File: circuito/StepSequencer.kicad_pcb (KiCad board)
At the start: 2 copper layers, 83 parts, among them P1 BEAGLEBONE_BLACK, SW1 SW_PUSH, SW10 SW_PUSH, SW11 SW_PUSH, SW12 SW_PUSH, SW13 SW_PUSH, SW14 SW_PUSH, SW15 SW_PUSH, SW16 SW_PUSH, SW2 SW_PUSH, SW3 SW_PUSH, SW4 SW_PUSH, SW5 SW_PUSH, SW6 SW_PUSH, SW7 SW_PUSH, SW8 SW_PUSH, SW9 SW_PUSH

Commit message: Empezando layout del pcb
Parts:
- removed D1, D10, D11, D12, D13, D14, D15, D16, D17, D18, D19, D2, D20, D21, D22, D23, D24, D25, D26, D27, D28, D29, D3, D30, D31, D32, D4, D5, D6, D7, D8, D9: LED, LEDs:LED-5MM
- removed R1, R10, R11, R12, R13, R14, R15, R16, R17, R18, R19, R2, R20, R21, R22, R23, R24, R25, R26, R27, R28, R29, R3, R30, R31, R32, R4, R5, R6, R7, R8, R9: R, Resistors_ThroughHole:Resistor_Horizontal_RM10mm
- removed SW16: SW_PUSH, Buttons_Switches_ThroughHole:SW_PUSH-12mm
- added D1_0 (x2): LED, LEDs:LED-5MM, F.Cu at (157.2, 152.4)
- added D1_1: LED, LEDs:LED-5MM, F.Cu at (170.0, 153.0)
- added D1_10, D1_11, D1_12, D1_8, D1_9: LED, LEDs:LED-5MM, F.Cu at (128.7, 83.1)
- added D1_13: LED, LEDs:LED-5MM, F.Cu at (128.0, 84.0)
- added D1_14, D1_15: LED, LEDs:LED-5MM, F.Cu at (130.0, 84.0)
- added D1_2: LED, LEDs:LED-5MM, F.Cu at (183.0, 152.0)
- added D1_3: LED, LEDs:LED-5MM, F.Cu at (197.0, 153.0)
- added D1_4: LED, LEDs:LED-5MM, F.Cu at (211.0, 152.0)
- added D1_5: LED, LEDs:LED-5MM, F.Cu at (225.0, 152.0)
- added D1_6: LED, LEDs:LED-5MM, F.Cu at (239.0, 152.0)
- added D1_7: LED, LEDs:LED-5MM, F.Cu at (253.0, 152.0)
- added D2_0: LED, LEDs:LED-5MM, F.Cu at (123.0, 154.0)
- added D2_1, D2_10, D2_11, D2_12, D2_13, D2_14, D2_15, D2_2, D2_3, D2_4, D2_5, D2_6, D2_7, D2_8, D2_9: LED, LEDs:LED-5MM, F.Cu at (128.8, 83.5)
- added R1_0: R, Resistors_ThroughHole:Resistor_Horizontal_RM10mm, F.Cu at (156.0, 157.2)
- added R1_1: R, Resistors_ThroughHole:Resistor_Horizontal_RM10mm, F.Cu at (171.0, 157.0)
- added R1_10, R1_11, R1_12, R1_13, R1_14, R1_15, R1_8, R1_9, R2_1, R2_10, R2_11, R2_12, R2_13, R2_14, R2_15, R2_2, R2_3, R2_4, R2_5, R2_6, R2_7, R2_8, R2_9: R, Resistors_ThroughHole:Resistor_Horizontal_RM10mm, F.Cu at (127.0, 75.0)
- added R1_2: R, Resistors_ThroughHole:Resistor_Horizontal_RM10mm, F.Cu at (185.0, 157.0)
- added R1_3: R, Resistors_ThroughHole:Resistor_Horizontal_RM10mm, F.Cu at (199.0, 157.0)
- added R1_4: R, Resistors_ThroughHole:Resistor_Horizontal_RM10mm, F.Cu at (212.0, 157.0)
- added R1_5: R, Resistors_ThroughHole:Resistor_Horizontal_RM10mm, F.Cu at (227.0, 157.0)
- added R1_6: R, Resistors_ThroughHole:Resistor_Horizontal_RM10mm, F.Cu at (240.0, 157.0)
- added R1_7: R, Resistors_ThroughHole:Resistor_Horizontal_RM10mm, F.Cu at (254.0, 157.0)
- added R2_0: R, Resistors_ThroughHole:Resistor_Horizontal_RM10mm, F.Cu at (122.0, 148.2)
- added SW0: SW_PUSH, Buttons_Switches_ThroughHole:SW_PUSH-12mm, F.Cu at (156.0, 140.8)
- RV1, RV2: footprint Potentiometers:Potentiometer_Alps-RK163-single_20mm -> StepSequencer:POT_AZUL
- moved RV1 124.6 mm to (99.5, 32.5)
- moved RV2 117.8 mm to (79.2, 32.5)
- moved SW2 103.4 mm to (169.9, 140.8), turned to 90 degrees
- moved P1 92.9 mm to (158.0, 126.0), turned to 0 degrees
- moved SW4 84.9 mm to (183.9, 140.8), turned to 90 degrees
- moved SW15 72.5 mm to (252.0, 98.9), turned to 90 degrees
- moved SW6 67.1 mm to (197.8, 140.8), turned to 90 degrees
- moved SW1 66.3 mm to (154.2, 98.9), turned to 90 degrees
- moved SW13 52.8 mm to (238.0, 98.9), turned to 90 degrees
- moved SW8 50.8 mm to (211.8, 140.8), turned to 90 degrees
- moved SW3 46.6 mm to (168.1, 98.9), turned to 90 degrees
- moved SW14 38.8 mm to (253.7, 140.8), turned to 90 degrees
- moved SW10 38.0 mm to (225.8, 140.8), turned to 90 degrees
- moved SW11 33.3 mm to (224.0, 98.9), turned to 90 degrees
- moved SW12 32.9 mm to (239.8, 140.8), turned to 90 degrees
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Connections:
- P1 pad A10: /led1_2 -> /led1_1
- P1 pad A11: /btn3 -> /btn2
- P1 pad A12: /led1_3 -> /led1_2
- P1 pad A13: /btn4 -> /btn3
- P1 pad A14: /led1_4 -> /led1_3
- P1 pad A15: /btn5 -> /btn4
- P1 pad A16: /led1_5 -> /led1_4
- P1 pad A17: /btn6 -> /btn5
- P1 pad A18: /led1_6 -> /led1_5
- P1 pad A19: /btn7 -> /btn6
- P1 pad A26: /led1_7 -> /led1_6
- P1 pad A27: /btn8 -> /btn7
- P1 pad A28: /led1_8 -> /led1_7
- P1 pad A29: /btn9 -> /btn8
- P1 pad A30: /led1_9 -> /led1_8
- P1 pad A31: /btn10 -> /btn9
- P1 pad A32: /led1_10 -> /led1_9
- P1 pad A33: /btn11 -> /btn10
- P1 pad A34: /led1_11 -> /led1_10
- P1 pad A35: /btn12 -> /btn11
- P1 pad A36: /led1_12 -> /led1_11
- P1 pad A37: /btn13 -> /btn12
- P1 pad A38: /led1_13 -> /led1_12
- P1 pad A39: /btn14 -> /btn13
- P1 pad A40: /led1_14 -> /led1_13
- P1 pad A41: /btn15 -> /btn14
- P1 pad A42: /led1_15 -> /led1_14
- P1 pad A43: /btn16 -> /btn15
- P1 pad A44: /led1_16 -> /led1_15
- P1 pad A7: /btn1 -> /btn0
- P1 pad A8: /led1_1 -> /led1_0
- P1 pad A9: /btn2 -> /btn1
- P1 pad B11: /led2_1 -> /led2_0
- P1 pad B12: /led2_9 -> /led2_8
- P1 pad B13: /led2_2 -> /led2_1
- P1 pad B14: /led2_10 -> /led2_9
- P1 pad B15: /led2_3 -> /led2_2
- P1 pad B16: /led2_11 -> /led2_10
- P1 pad B17: /led2_4 -> /led2_3
- P1 pad B18: /led2_12 -> /led2_11
- P1 pad B21: /led2_5 -> /led2_4
- P1 pad B22: /led2_13 -> /led2_12
- P1 pad B23: /led2_6 -> /led2_5
- P1 pad B24: /led2_14 -> /led2_13
- P1 pad B26: /led2_15 -> /led2_14
- P1 pad B27: /led2_7 -> /led2_6
- P1 pad B30: /led2_16 -> /led2_15
- P1 pad B38: /pot2 -> /pot1
- P1 pad B40: /pot1 -> /pot0
- P1 pad B41: /led2_8 -> /led2_7
- RV1 pad 2: /pot1 -> /pot0
- RV2 pad 2: /pot2 -> /pot1

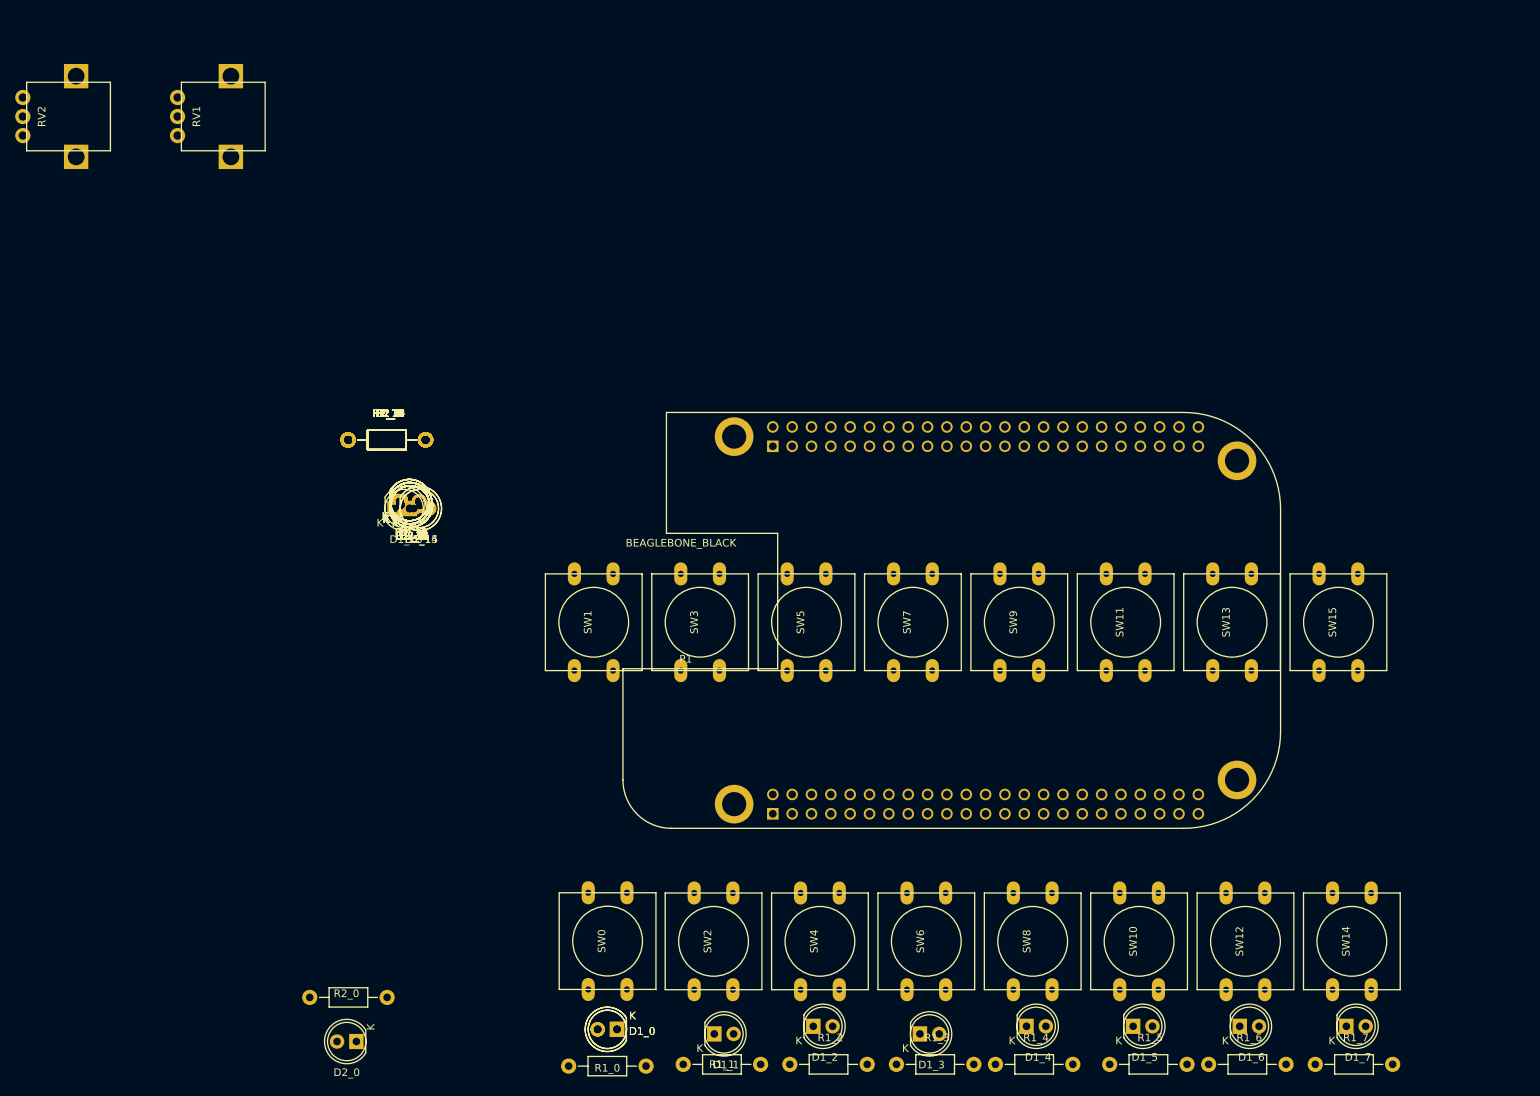
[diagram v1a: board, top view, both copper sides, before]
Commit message: PBC ruteado de leds, botones, beagle, faltan pots y tierras.
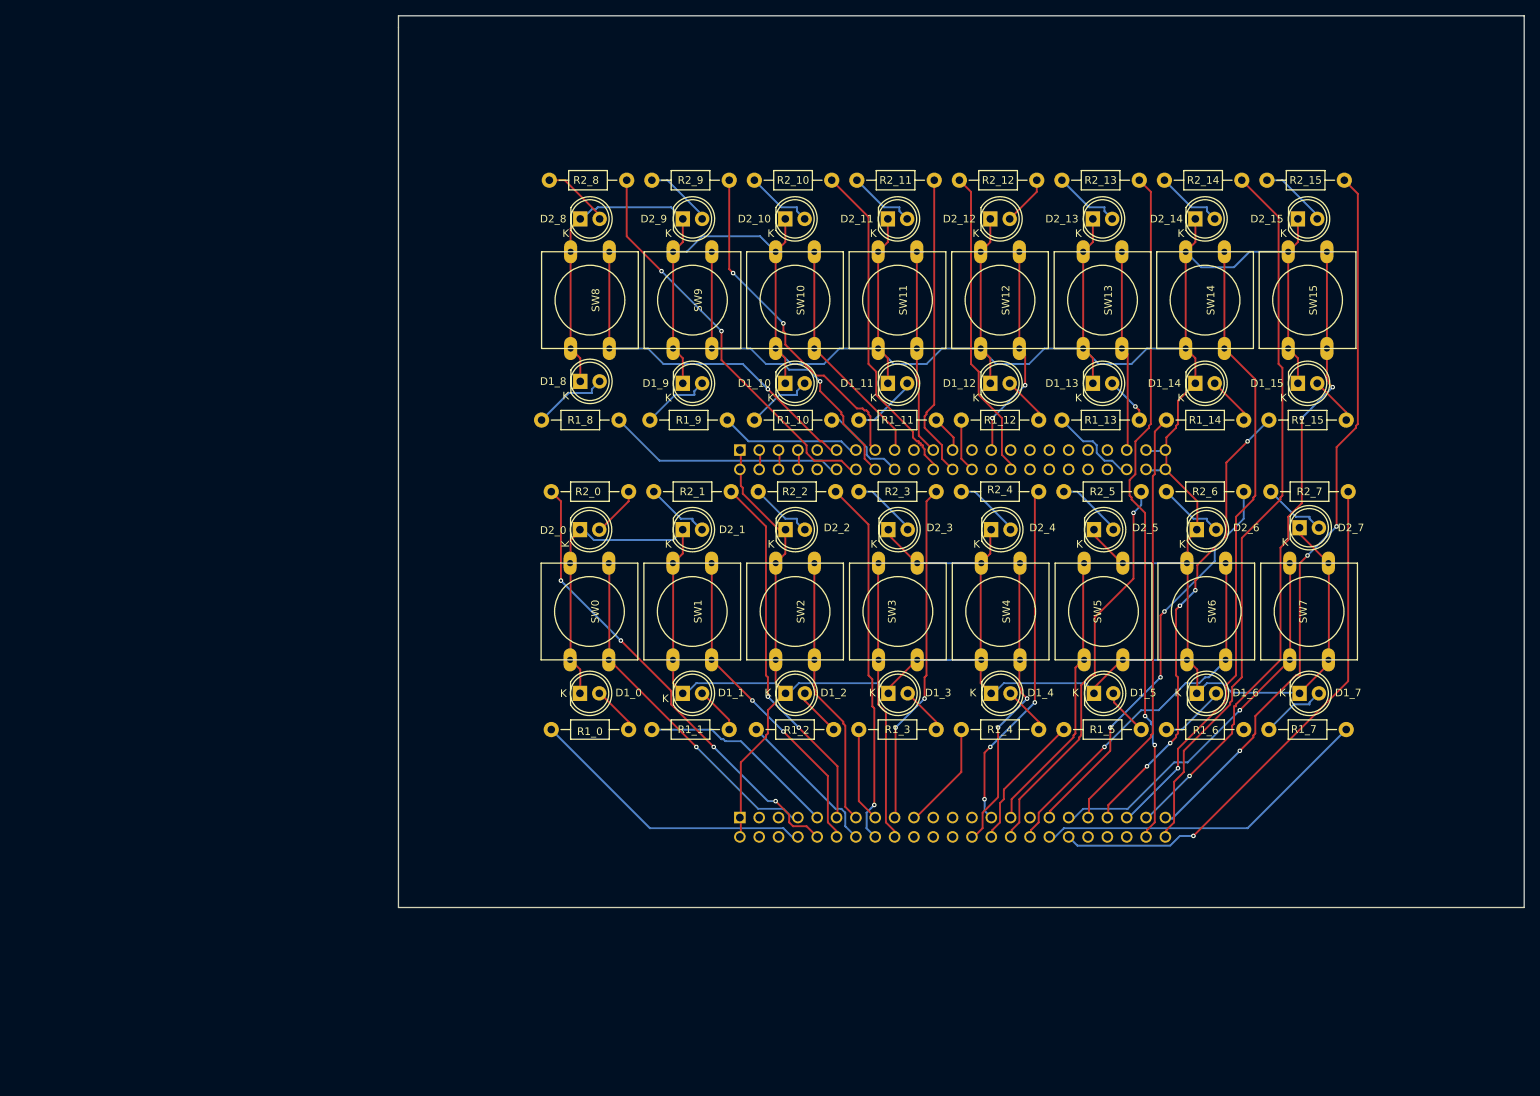
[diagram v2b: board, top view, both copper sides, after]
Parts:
- removed the D1_0 at (157.2, 152.4)
- removed RV1, RV2: POT, StepSequencer:POT_AZUL
- P1: footprint beagleboard:BEAGLEBONE_BLACK -> StepSequencer:BEAGLEBONE_BLACK; moved to B.Cu
- moved R2_15 125.4 mm to (247.7, 40.9)
- moved D2_15 123.7 mm to (246.6, 46.0)
- moved R2_7 121.3 mm to (248.2, 81.8)
- moved R1_15 120.9 mm to (247.9, 72.4), turned to 180 degrees
- moved D2_7 118.1 mm to (246.9, 86.5)
- moved D1_15 117.8 mm to (246.6, 67.6)
- moved R2_14 112.5 mm to (234.2, 40.9)
- moved D2_14 110.9 mm to (233.2, 46.0)
- moved R2_6 107.7 mm to (234.4, 81.8)
- moved R1_14 107.5 mm to (234.4, 72.4), turned to 180 degrees
- moved D2_6 104.6 mm to (233.4, 86.8)
- moved D1_14 104.5 mm to (233.2, 67.6)
- moved SW8 102.3 mm to (153.7, 56.6), turned to 270 degrees
- moved R2_13 99.7 mm to (220.7, 40.9)
- moved D2_13 98.4 mm to (219.7, 46.0)
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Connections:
- D1_0 pad 1: Net-(D1_0-Pad1) -> GNDD
- D1_0 pad 2: +3V3 -> Net-(D1_0-Pad2)
- D1_1 pad 1: Net-(D1_1-Pad1) -> GNDD
- D1_1 pad 2: +3V3 -> Net-(D1_1-Pad2)
- D1_10 pad 1: Net-(D1_10-Pad1) -> GNDD
- D1_10 pad 2: +3V3 -> Net-(D1_10-Pad2)
- D1_11 pad 1: Net-(D1_11-Pad1) -> GNDD
- D1_11 pad 2: +3V3 -> Net-(D1_11-Pad2)
- D1_12 pad 1: Net-(D1_12-Pad1) -> GNDD
- D1_12 pad 2: +3V3 -> Net-(D1_12-Pad2)
- D1_13 pad 1: Net-(D1_13-Pad1) -> GNDD
- D1_13 pad 2: +3V3 -> Net-(D1_13-Pad2)
- D1_14 pad 1: Net-(D1_14-Pad1) -> GNDD
- D1_14 pad 2: +3V3 -> Net-(D1_14-Pad2)
- D1_15 pad 1: Net-(D1_15-Pad1) -> GNDD
- D1_15 pad 2: +3V3 -> Net-(D1_15-Pad2)
- D1_2 pad 1: Net-(D1_2-Pad1) -> GNDD
- D1_2 pad 2: +3V3 -> Net-(D1_2-Pad2)
- D1_3 pad 1: Net-(D1_3-Pad1) -> GNDD
- D1_3 pad 2: +3V3 -> Net-(D1_3-Pad2)
- D1_4 pad 1: Net-(D1_4-Pad1) -> GNDD
- D1_4 pad 2: +3V3 -> Net-(D1_4-Pad2)
- D1_5 pad 1: Net-(D1_5-Pad1) -> GNDD
- D1_5 pad 2: +3V3 -> Net-(D1_5-Pad2)
- D1_6 pad 1: Net-(D1_6-Pad1) -> GNDD
- D1_6 pad 2: +3V3 -> Net-(D1_6-Pad2)
- D1_7 pad 1: Net-(D1_7-Pad1) -> GNDD
- D1_7 pad 2: +3V3 -> Net-(D1_7-Pad2)
- D1_8 pad 1: Net-(D1_8-Pad1) -> GNDD
- D1_8 pad 2: +3V3 -> Net-(D1_8-Pad2)
- D1_9 pad 1: Net-(D1_9-Pad1) -> GNDD
- D1_9 pad 2: +3V3 -> Net-(D1_9-Pad2)
- D2_0 pad 1: Net-(D2_0-Pad1) -> GNDD
- D2_0 pad 2: +3V3 -> Net-(D2_0-Pad2)
- D2_1 pad 1: Net-(D2_1-Pad1) -> GNDD
- D2_1 pad 2: +3V3 -> Net-(D2_1-Pad2)
- D2_10 pad 1: Net-(D2_10-Pad1) -> GNDD
- D2_10 pad 2: +3V3 -> Net-(D2_10-Pad2)
- D2_11 pad 1: Net-(D2_11-Pad1) -> GNDD
- D2_11 pad 2: +3V3 -> Net-(D2_11-Pad2)
- D2_12 pad 1: Net-(D2_12-Pad1) -> GNDD
- D2_12 pad 2: +3V3 -> Net-(D2_12-Pad2)
- D2_13 pad 1: Net-(D2_13-Pad1) -> GNDD
- D2_13 pad 2: +3V3 -> Net-(D2_13-Pad2)
- D2_14 pad 1: Net-(D2_14-Pad1) -> GNDD
- D2_14 pad 2: +3V3 -> Net-(D2_14-Pad2)
- D2_15 pad 1: Net-(D2_15-Pad1) -> GNDD
- D2_15 pad 2: +3V3 -> Net-(D2_15-Pad2)
- D2_2 pad 1: Net-(D2_2-Pad1) -> GNDD
- D2_2 pad 2: +3V3 -> Net-(D2_2-Pad2)
- D2_3 pad 1: Net-(D2_3-Pad1) -> GNDD
- D2_3 pad 2: +3V3 -> Net-(D2_3-Pad2)
- D2_4 pad 1: Net-(D2_4-Pad1) -> GNDD
- D2_4 pad 2: +3V3 -> Net-(D2_4-Pad2)
- D2_5 pad 1: Net-(D2_5-Pad1) -> GNDD
- D2_5 pad 2: +3V3 -> Net-(D2_5-Pad2)
- D2_6 pad 1: Net-(D2_6-Pad1) -> GNDD
- D2_6 pad 2: +3V3 -> Net-(D2_6-Pad2)
- D2_7 pad 1: Net-(D2_7-Pad1) -> GNDD
- D2_7 pad 2: +3V3 -> Net-(D2_7-Pad2)
- D2_8 pad 1: Net-(D2_8-Pad1) -> GNDD
- D2_8 pad 2: +3V3 -> Net-(D2_8-Pad2)
- D2_9 pad 1: Net-(D2_9-Pad1) -> GNDD
- D2_9 pad 2: +3V3 -> Net-(D2_9-Pad2)
- P1 pad A1: Net-(P1-PadA1) -> GNDD
- P1 pad A10: /led1_1 -> /led2_0
- P1 pad A11: /btn2 -> /led2_1
- P1 pad A12: /led1_2 -> /btn1
- P1 pad A13: /btn3 -> /btn2
- P1 pad A14: /led1_3 -> /led1_2
- P1 pad A15: /btn4 -> /led1_3
- P1 pad A16: /led1_4 -> /led2_2
- P1 pad A17: /btn5 -> /led2_3
- P1 pad A18: /led1_5 -> /btn3
- P1 pad A19: /btn6 -> /led1_4
- P1 pad A2: Net-(P1-PadA2) -> GNDD
- P1 pad A20: Net-(P1-PadA20) -> (no net)
- P1 pad A21: Net-(P1-PadA21) -> (no net)
- P1 pad A22: Net-(P1-PadA22) -> (no net)
- P1 pad A23: Net-(P1-PadA23) -> (no net)
- P1 pad A24: Net-(P1-PadA24) -> (no net)
- P1 pad A25: Net-(P1-PadA25) -> (no net)
- P1 pad A26: /led1_6 -> /btn4
- P1 pad A27: /btn7 -> /led2_4
- P1 pad A28: /led1_7 -> /led1_5
- P1 pad A29: /btn8 -> /btn5
- P1 pad A3: Net-(P1-PadA3) -> (no net)
- P1 pad A30: /led1_8 -> /led2_5
- P1 pad A31: /btn9 -> (no net)
- P1 pad A32: /led1_9 -> /btn6
- P1 pad A33: /btn10 -> /led2_6
- P1 pad A34: /led1_10 -> /led1_7
- P1 pad A35: /btn11 -> /btn7
- P1 pad A36: /led1_11 -> /led2_7
- P1 pad A37: /btn12 -> /led1_14
- P1 pad A38: /led1_12 -> (no net)
- P1 pad A39: /btn13 -> /led1_15
- P1 pad A4: Net-(P1-PadA4) -> (no net)
- P1 pad A40: /led1_13 -> (no net)
- P1 pad A42: /led1_14 -> (no net)
- P1 pad A44: /led1_15 -> /led2_13
- P1 pad A45: /unused -> /led2_15
- P1 pad A46: /unused -> /led2_14
- P1 pad A5: Net-(P1-PadA5) -> (no net)
- P1 pad A6: Net-(P1-PadA6) -> (no net)
- P1 pad A9: /btn1 -> /led1_1
- P1 pad B1: /GND -> GNDD
- P1 pad B10: /SYS_RESETn -> (no net)
- P1 pad B11: /led2_0 -> /btn8
- P1 pad B12: /led2_8 -> /led1_8
- P1 pad B13: /led2_1 -> /led1_9
- P1 pad B14: /led2_9 -> /led2_8
- P1 pad B15: /led2_2 -> /led2_9
- P1 pad B16: /led2_10 -> /btn9
- P1 pad B17: /led2_3 -> /btn10
- P1 pad B18: /led2_11 -> /led1_10
- P1 pad B19: Net-(P1-PadB19) -> (no net)
- P1 pad B2: /GND -> GNDD
- P1 pad B20: Net-(P1-PadB20) -> (no net)
- P1 pad B21: /led2_4 -> /btn11
- P1 pad B22: /led2_12 -> /led2_10
- P1 pad B23: /led2_5 -> /led1_11
- P1 pad B24: /led2_13 -> /led2_11
- P1 pad B25: Net-(P1-PadB25) -> (no net)
- P1 pad B26: /led2_14 -> /led1_12
- P1 pad B27: /led2_6 -> /btn12
- P1 pad B28: Net-(P1-PadB28) -> (no net)
- P1 pad B29: Net-(P1-PadB29) -> (no net)
- P1 pad B3: /DC_3.3V -> +3V3
- P1 pad B30: /led2_15 -> /led2_12
- P1 pad B31: Net-(P1-PadB31) -> (no net)
- P1 pad B33: /AIN4 -> (no net)
- P1 pad B35: /AIN6 -> (no net)
- P1 pad B36: /AIN5 -> (no net)
- P1 pad B37: /AIN2 -> (no net)
- P1 pad B38: /pot1 -> (no net)
- P1 pad B39: /AIN0 -> (no net)
- P1 pad B4: /DC_3.3V -> +3V3
- P1 pad B40: /pot0 -> (no net)
- P1 pad B41: /led2_7 -> /btn13
- P1 pad B42: /GPIO0_7 -> /led1_13
- P1 pad B43: /GND -> GNDD
- P1 pad B44: /GND -> GNDD
- P1 pad B45: /GND -> GNDD
- P1 pad B46: /GND -> GNDD
- P1 pad B9: /PWR_BUT -> (no net)
- R1_0 pad 1: Net-(D1_0-Pad1) -> Net-(D1_0-Pad2)
- R1_1 pad 1: Net-(D1_1-Pad1) -> Net-(D1_1-Pad2)
- R1_10 pad 1: Net-(D1_10-Pad1) -> Net-(D1_10-Pad2)
- R1_11 pad 1: Net-(D1_11-Pad1) -> Net-(D1_11-Pad2)
- R1_12 pad 1: Net-(D1_12-Pad1) -> Net-(D1_12-Pad2)
- R1_13 pad 1: Net-(D1_13-Pad1) -> Net-(D1_13-Pad2)
- R1_14 pad 1: Net-(D1_14-Pad1) -> Net-(D1_14-Pad2)
- R1_15 pad 1: Net-(D1_15-Pad1) -> Net-(D1_15-Pad2)
- R1_2 pad 1: Net-(D1_2-Pad1) -> Net-(D1_2-Pad2)
- R1_3 pad 1: Net-(D1_3-Pad1) -> Net-(D1_3-Pad2)
- R1_4 pad 1: Net-(D1_4-Pad1) -> Net-(D1_4-Pad2)
- R1_5 pad 1: Net-(D1_5-Pad1) -> Net-(D1_5-Pad2)
- R1_6 pad 1: Net-(D1_6-Pad1) -> Net-(D1_6-Pad2)
- R1_6 pad 2: /led1_6. -> (no net)
- R1_7 pad 1: Net-(D1_7-Pad1) -> Net-(D1_7-Pad2)
- R1_8 pad 1: Net-(D1_8-Pad1) -> Net-(D1_8-Pad2)
- R1_9 pad 1: Net-(D1_9-Pad1) -> Net-(D1_9-Pad2)
- R2_0 pad 1: Net-(D2_0-Pad1) -> Net-(D2_0-Pad2)
- R2_1 pad 1: Net-(D2_1-Pad1) -> Net-(D2_1-Pad2)
- R2_10 pad 1: Net-(D2_10-Pad1) -> Net-(D2_10-Pad2)
- R2_11 pad 1: Net-(D2_11-Pad1) -> Net-(D2_11-Pad2)
- R2_12 pad 1: Net-(D2_12-Pad1) -> Net-(D2_12-Pad2)
- R2_13 pad 1: Net-(D2_13-Pad1) -> Net-(D2_13-Pad2)
- R2_14 pad 1: Net-(D2_14-Pad1) -> Net-(D2_14-Pad2)
- R2_15 pad 1: Net-(D2_15-Pad1) -> Net-(D2_15-Pad2)
- R2_2 pad 1: Net-(D2_2-Pad1) -> Net-(D2_2-Pad2)
- R2_3 pad 1: Net-(D2_3-Pad1) -> Net-(D2_3-Pad2)
- R2_4 pad 1: Net-(D2_4-Pad1) -> Net-(D2_4-Pad2)
- R2_5 pad 1: Net-(D2_5-Pad1) -> Net-(D2_5-Pad2)
- R2_6 pad 1: Net-(D2_6-Pad1) -> Net-(D2_6-Pad2)
- R2_7 pad 1: Net-(D2_7-Pad1) -> Net-(D2_7-Pad2)
- R2_8 pad 1: Net-(D2_8-Pad1) -> Net-(D2_8-Pad2)
- R2_9 pad 1: Net-(D2_9-Pad1) -> Net-(D2_9-Pad2)
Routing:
- net GNDD: track 0.00 -> 623.7 mm
- net /led2_15: track 0.00 -> 95.9 mm, vias 0 -> 3
- net /led2_14: track 0.00 -> 95.1 mm
- net /led2_13: track 0.00 -> 90.1 mm, vias 0 -> 2
- net /btn15: track 0.00 -> 85.0 mm, vias 0 -> 3
- net /btn14: track 0.00 -> 83.2 mm, vias 0 -> 1
- net /led2_7: track 0.00 -> 71.0 mm, vias 0 -> 1
- net /led1_15: track 0.00 -> 61.4 mm, vias 0 -> 5
- net /led2_0: track 0.00 -> 61.4 mm, vias 0 -> 4
- net /led1_14: track 0.00 -> 56.7 mm
- net /led2_6: track 0.00 -> 53.6 mm, vias 0 -> 3
- net /led2_8: track 0.00 -> 53.3 mm, vias 0 -> 2
- net /led2_5: track 0.00 -> 53.0 mm, vias 0 -> 1
- net /btn7: track 0.00 -> 50.6 mm, vias 0 -> 1
- net /btn6: track 0.00 -> 49.8 mm, vias 0 -> 1
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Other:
- board outline added: 147.8 x 117.1 mm
